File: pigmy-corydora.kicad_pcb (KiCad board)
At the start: 2 copper layers, 2 parts, among them SW1 SW_Push, SW2 SW_Push

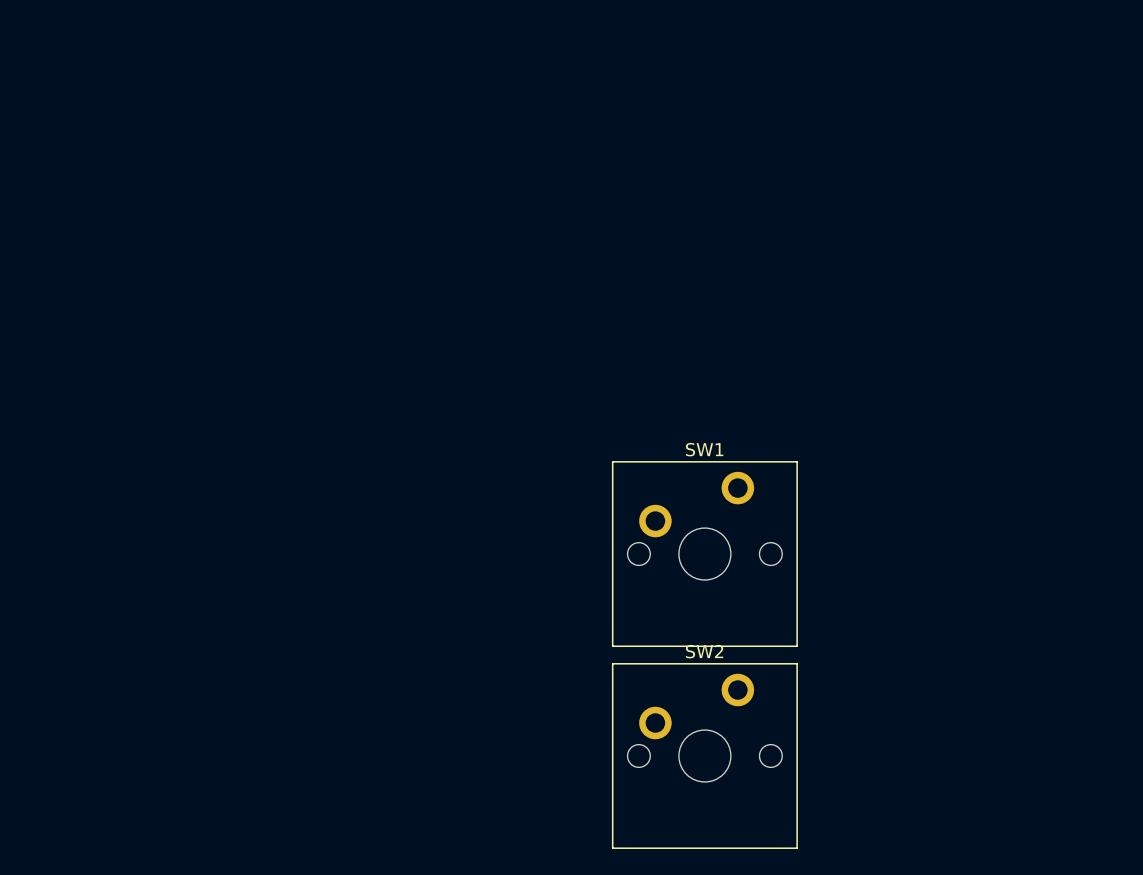
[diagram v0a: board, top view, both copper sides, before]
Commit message: feat: added mounting holes to PCB
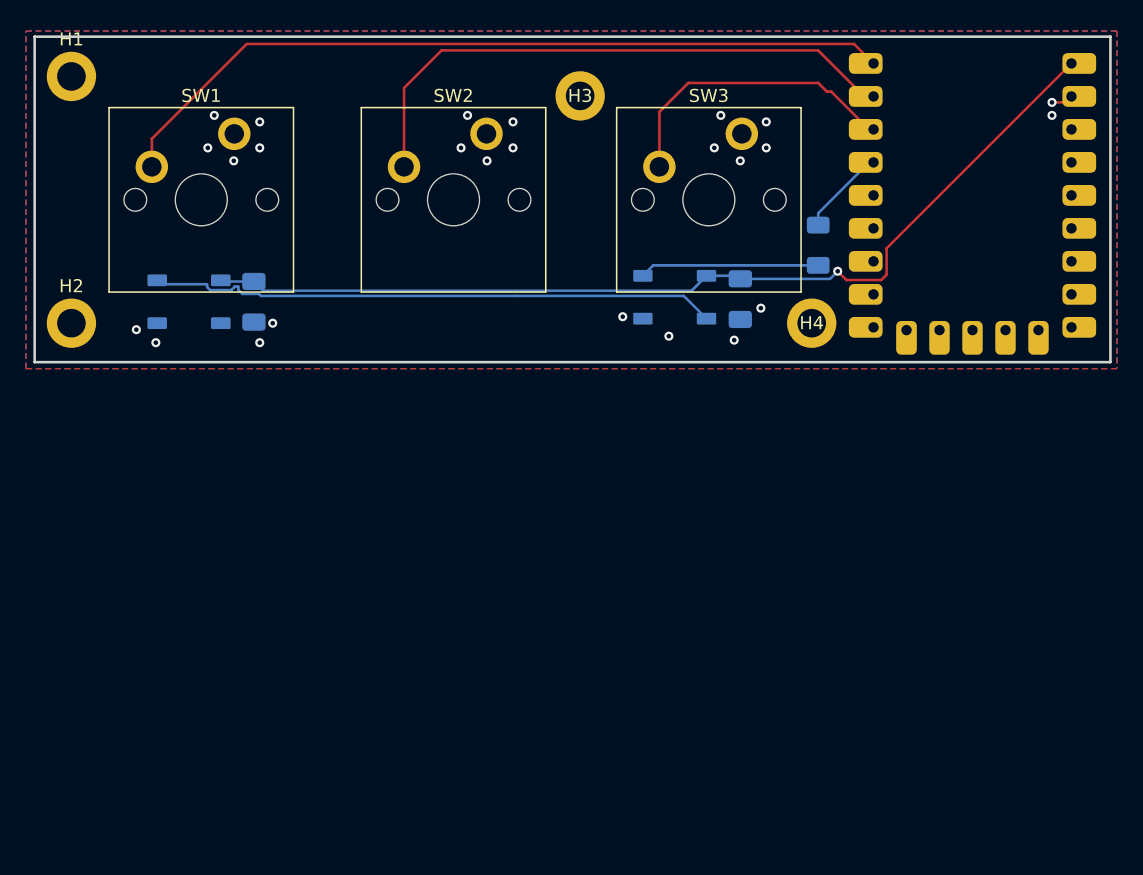
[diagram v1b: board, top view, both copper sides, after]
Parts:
- added C1: 0.1uF, Capacitor_SMD:C_1206_3216Metric_Pad1.33x1.80mm_HandSolder, B.Cu at (111.0, 54.9)
- added C2: 0.1uF, Capacitor_SMD:C_1206_3216Metric_Pad1.33x1.80mm_HandSolder, B.Cu at (148.5, 54.6)
- added D1: WS2812B, LED_SMD:LED_WS2812B_PLCC4_5.0x5.0mm_P3.2mm, B.Cu at (143.4, 54.5)
- added D2: WS2812B, LED_SMD:LED_WS2812B_PLCC4_5.0x5.0mm_P3.2mm, B.Cu at (106.0, 54.9)
- added H1: MountingHole, MountingHole:MountingHole_2.2mm_M2_DIN965_Pad, F.Cu at (97.0, 37.5)
- added H2: MountingHole, MountingHole:MountingHole_2.2mm_M2_DIN965_Pad, F.Cu at (97.0, 56.5)
- added H3: MountingHole, MountingHole:MountingHole_2.2mm_M2_DIN965_Pad, F.Cu at (136.2, 39.0)
- added H4: MountingHole, MountingHole:MountingHole_2.2mm_M2_DIN965_Pad, F.Cu at (154.0, 56.5)
- added R1: 330, Resistor_SMD:R_1206_3216Metric_Pad1.30x1.75mm_HandSolder, B.Cu at (154.5, 50.5)
- added RZ1: RP2040-Zero, rp2040-zero:RP2040-Zero, B.Cu at (176.5, 59.4)
- added SW3: SW_Push, PCM_Switch_Keyboard_Cherry_MX:SW_Cherry_MX_PCB_1.00u, F.Cu at (146.1, 47.0)
- moved SW1 47.4 mm to (107.0, 47.0)
- moved SW2 47.0 mm to (126.4, 47.0)
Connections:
- SW1 pad 1: unconnected-(SW1-Pad1) -> /SW1
- SW1 pad 2: unconnected-(SW1-Pad2) -> GND
- SW2 pad 1: unconnected-(SW2-Pad1) -> /SW2
- SW2 pad 2: unconnected-(SW2-Pad2) -> GND
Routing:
- net /VBUS: track 0.00 -> 75.0 mm, vias 0 -> 1
- net /SW1: track 0.00 -> 61.4 mm
- net /SW2: track 0.00 -> 44.9 mm
- net Net-(D1-DOUT): track 0.00 -> 44.0 mm
- net /SW3: track 0.00 -> 23.1 mm
- net Net-(D1-DIN): track 0.00 -> 13.8 mm
- net /WS2812: track 0.00 -> 6.80 mm
- net GND: track 0.00 -> 1.69 mm, vias 0 -> 25
- added copper zone on B.Cu, net GND
- added copper zone on F.Cu, net GND
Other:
- board outline added: 82.8 x 25.1 mm

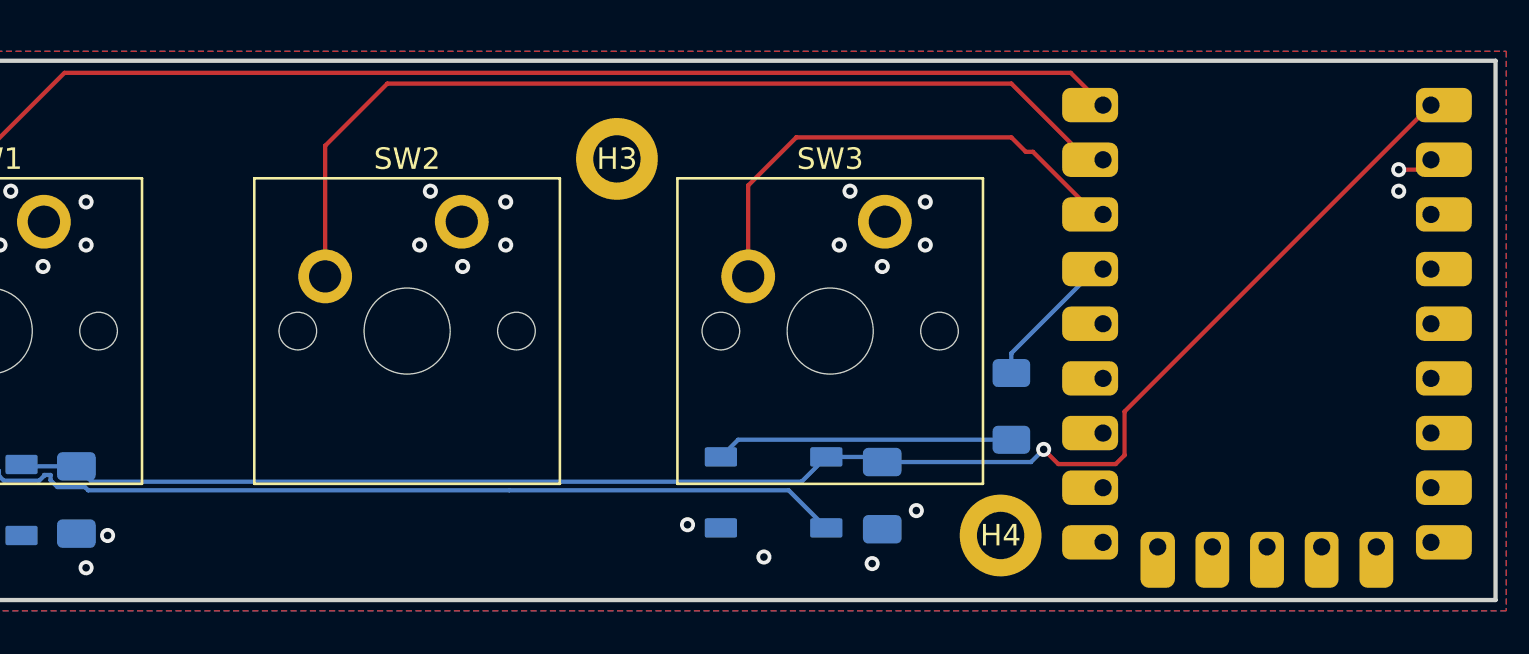
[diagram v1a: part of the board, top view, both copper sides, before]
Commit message: chore: created readme + added logos to pcb
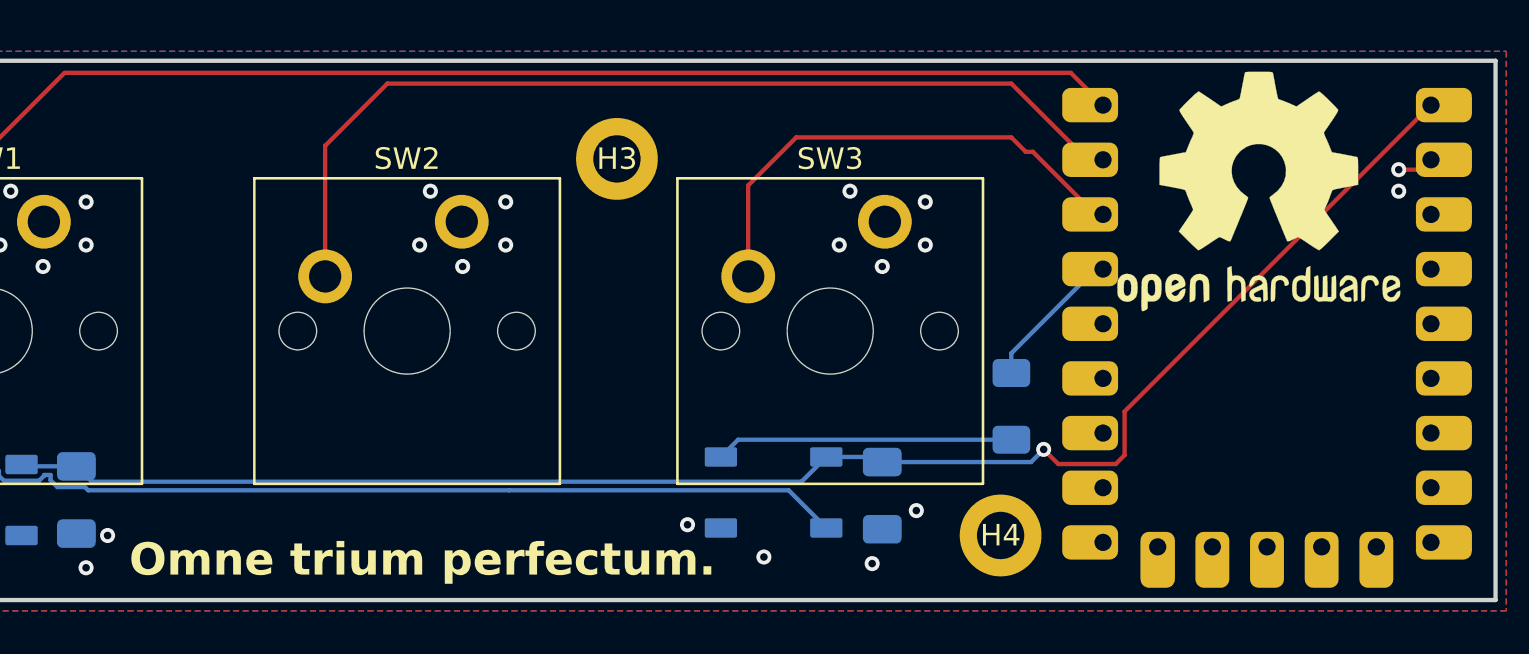
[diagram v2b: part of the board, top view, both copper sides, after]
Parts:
- added REF**: OSHW-Logo2_14.6x12mm_SilkScreen, Symbol:OSHW-Logo2_14.6x12mm_SilkScreen, F.Cu at (166.0, 40.5)
- added d: LOGO, KiCadLibrariesRoot:Tobe_logo, B.Cu at (118.0, 52.0)
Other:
- board text added: "Omne trium perfectum."
- board text added: "Pigmy CoryDora v1 github.com/balub/Pigmy-CoryDora"
